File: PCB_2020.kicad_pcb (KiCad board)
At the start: 2 copper layers, 109.5 x 88 mm, 27 parts, among them IC1 LM358N, Q1 100V/17A, Q2 100V/17A, Q3 100V/17A, Q4 100V/17A, Q5 100V/17A, Q6 100V/17A, U1 AMP_DUE_SCH

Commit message: Updating PCB
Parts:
- added G***: LOGO, Image:Silk_Small_P, F.Cu at (252.7, 103.9)

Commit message: Reworked PCB
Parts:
- removed G***: LOGO, Image:Silk_Small_P
- added C1: 0.022uF, Capacitor_SMD:C_0805_2012Metric_Pad1.18x1.45mm_HandSolder, F.Cu at (169.2, 85.7)
- added C3: 0.022uF, Capacitor_SMD:C_0805_2012Metric_Pad1.18x1.45mm_HandSolder, F.Cu at (169.2, 81.5)
- added R3: 1000, Resistor_SMD:R_0612_1632Metric_Pad1.18x3.40mm_HandSolder, F.Cu at (190.1, 101.7)
- added R4: 1000, Resistor_SMD:R_0612_1632Metric_Pad1.18x3.40mm_HandSolder, F.Cu at (192.5, 133.3)
- added R6: 5400, Resistor_SMD:R_0612_1632Metric_Pad1.18x3.40mm_HandSolder, F.Cu at (201.7, 102.0)
- added R7: 5400, Resistor_SMD:R_0612_1632Metric_Pad1.18x3.40mm_HandSolder, F.Cu at (192.4, 122.4)
- added R8: 5000, Resistor_SMD:R_0612_1632Metric_Pad1.18x3.40mm_HandSolder, F.Cu at (196.9, 133.3)
- added R9: 1000, Resistor_SMD:R_0612_1632Metric_Pad1.18x3.40mm_HandSolder, F.Cu at (195.5, 101.4)
- added U2: TL084CN, Drivetrain_control:TL084CN, F.Cu at (194.3, 113.9)
- added U3: DRV8874, Drivetrain_control:DRV8874PWPR, F.Cu at (176.9, 82.9)
- C2, C5: footprint Capacitor_SMD:C_0805_2012Metric_Pad1.15x1.40mm_HandSolder -> Capacitor_SMD:C_0805_2012Metric_Pad1.18x1.45mm_HandSolder
- R1, R18, R2, R5: footprint Resistor_SMD:R_0805_2012Metric_Pad1.15x1.40mm_HandSolder -> Resistor_SMD:R_0612_1632Metric_Pad1.18x3.40mm_HandSolder
- moved CONN6 84.2 mm to (170.6, 77.4)
- moved C1 81.5 mm to (160.8, 88.3)
- moved C2 81.5 mm to (179.6, 115.1)
- moved C5 81.5 mm to (141.6, 89.1)
- moved CONN2 81.5 mm to (174.8, 110.6)
- moved CONN3 81.5 mm to (160.3, 65.1)
- moved CONN4 81.5 mm to (151.6, 60.0)
- moved CONN5 81.5 mm to (169.1, 118.6)
- moved CONN7 81.5 mm to (169.1, 65.1)
- moved H1 81.5 mm to (176.3, 135.8)
- moved H3 81.5 mm to (176.3, 58.9)
- moved IC1 81.5 mm to (145.1, 82.6)
- moved Q1 81.5 mm to (177.6, 119.3)
- moved Q2 81.5 mm to (164.1, 108.1)
- moved Q3 81.5 mm to (156.3, 108.3)
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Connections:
- U1 pad 1: (no net) -> Net-(U1-Pad1)
- U1 pad 10: (no net) -> Net-(U1-Pad10)
- U1 pad 11: (no net) -> Net-(U1-Pad11)
- U1 pad 12: (no net) -> Net-(U1-Pad12)
- U1 pad 13: (no net) -> Net-(U1-Pad13)
- U1 pad 14: (no net) -> Net-(U1-Pad14)
- U1 pad 15: (no net) -> Net-(U1-Pad15)
- U1 pad 16: (no net) -> Net-(U1-Pad16)
- U1 pad 17: (no net) -> Net-(U1-Pad17)
- U1 pad 18: (no net) -> Brake_PWM_1
- U1 pad 19: (no net) -> Brake_PWM_2
- U1 pad 2: (no net) -> Net-(U1-Pad2)
- U1 pad 20: (no net) -> STEERING
- U1 pad 21: THROTTLE -> Net-(U1-Pad21)
- U1 pad 22: (no net) -> Net-(U1-Pad22)
- U1 pad 23: (no net) -> Net-(U1-Pad23)
- U1 pad 24: (no net) -> +12V
- U1 pad 25: (no net) -> Net-(U1-Pad25)
- U1 pad 26: (no net) -> Net-(U1-Pad26)
- U1 pad 27: (no net) -> Net-(U1-Pad27)
- U1 pad 28: (no net) -> SCIB_TX
- U1 pad 29: (no net) -> Net-(U1-Pad29)
- U1 pad 3: (no net) -> Net-(U1-Pad3)
- U1 pad 30: (no net) -> Net-(U1-Pad30)
- U1 pad 31: (no net) -> Net-(U1-Pad31)
- U1 pad 32: (no net) -> Net-(U1-Pad32)
- U1 pad 33: (no net) -> Net-(U1-Pad33)
- U1 pad 34: (no net) -> THROTTLE
- U1 pad 35: (no net) -> Net-(U1-Pad35)
- U1 pad 36: (no net) -> SCIB_RX
- U1 pad 37: (no net) -> Net-(U1-Pad37)
- U1 pad 38: (no net) -> Net-(U1-Pad38)
- U1 pad 39: (no net) -> Net-(U1-Pad39)
- U1 pad 4: (no net) -> Net-(U1-Pad4)
- U1 pad 40: (no net) -> Net-(U1-Pad40)
- U1 pad 41: (no net) -> GND
- U1 pad 42: (no net) -> GND
- U1 pad 43: (no net) -> Net-(U1-Pad43)
- U1 pad 44: REV_CTL -> Net-(U1-Pad44)
- U1 pad 45: (no net) -> Net-(U1-Pad45)
- U1 pad 46: (no net) -> INPUT_A+_CTL
- U1 pad 47: EN+_CTL -> Net-(U1-Pad47)
- U1 pad 48: (no net) -> Net-(U1-Pad48)
- U1 pad 49: (no net) -> Net-(U1-Pad49)
- U1 pad 5: +5V -> Net-(U1-Pad5)
- U1 pad 50: INPUT_A+_CTL -> Net-(U1-Pad50)
- U1 pad 51: (no net) -> Net-(U1-Pad51)
- U1 pad 52: (no net) -> Net-(U1-Pad52)
- U1 pad 53: FS1_CTL -> EN+_CTL
- U1 pad 54: (no net) -> Net-(U1-Pad54)
- U1 pad 55: (no net) -> Net-(U1-Pad55)
- U1 pad 56: FWD_CTL -> Net-(U1-Pad56)
- U1 pad 57: (no net) -> Net-(U1-Pad57)
- U1 pad 58: (no net) -> Net-(U1-Pad58)
- U1 pad 59: (no net) -> REV_CTL
- U1 pad 6: GND -> Net-(U1-Pad6)
- U1 pad 60: (no net) -> Net-(U1-Pad60)
- U1 pad 61: (no net) -> Net-(U1-Pad61)
- U1 pad 62: (no net) -> Net-(U1-Pad62)
- U1 pad 63: (no net) -> Net-(U1-Pad63)
- U1 pad 64: STEERING -> Net-(U1-Pad64)
- U1 pad 65: Brake_PWM_2 -> Net-(U1-Pad65)
- U1 pad 66: Brake_PWM_1 -> +5V
- U1 pad 67: (no net) -> KS1_CTL
- U1 pad 68: (no net) -> Net-(U1-Pad68)
- U1 pad 69: (no net) -> Net-(U1-Pad69)
- U1 pad 7: GND -> Net-(U1-Pad7)
- U1 pad 70: (no net) -> Net-(U1-Pad70)
- U1 pad 71: (no net) -> Net-(U1-Pad71)
- U1 pad 72: (no net) -> Net-(U1-Pad72)
- U1 pad 73: (no net) -> Net-(U1-Pad73)
- U1 pad 74: (no net) -> FWD_CTL
- U1 pad 75: (no net) -> Net-(U1-Pad75)
- U1 pad 76: (no net) -> Net-(U1-Pad76)
- U1 pad 77: (no net) -> Net-(U1-Pad77)
- U1 pad 78: (no net) -> Net-(U1-Pad78)
- U1 pad 79: (no net) -> Net-(U1-Pad79)
- U1 pad 8: +12V -> Net-(U1-Pad8)
- U1 pad 80: (no net) -> FS1_CTL
- U1 pad 81: (no net) -> Net-(U1-Pad81)
- U1 pad 82: (no net) -> Net-(U1-Pad82)
- U1 pad 83: (no net) -> Net-(U1-Pad83)
- U1 pad 84: (no net) -> Net-(U1-Pad84)
- U1 pad 85: (no net) -> Net-(U1-Pad85)
- U1 pad 9: (no net) -> Net-(U1-Pad9)
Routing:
- net FS1_CTL: track 50.9 -> 184.6 mm
- net THROTTLE: track 36.3 -> 158.3 mm
- net +3V3: track 110.1 -> 221.5 mm
- net INPUT_A+_CTL: track 64.9 -> 135.2 mm
- net STEERING: track 119.8 -> 51.5 mm
- net FWD_CTL: track 66.9 -> 134.5 mm
- net +5V: track 18.2 -> 78.4 mm
- net Net-(R3-Pad2): track 0.00 -> 55.2 mm
- net Net-(R4-Pad1): track 0.00 -> 46.8 mm
- net REV_CTL: track 39.6 -> 78.1 mm
- net GND: track 10.9 -> 46.6 mm, vias 4 -> 10
- net EN+_CTL: track 51.4 -> 83.9 mm
- net /LAUNCHXL-F28379D Breakout/THROTTLE_MC: track 48.6 -> 80.7 mm
- net Net-(R3-Pad1): track 0.00 -> 27.6 mm
- net /LAUNCHXL-F28379D Breakout/Brake_Out_2: track 16.3 -> 28.6 mm
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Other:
- board size 109.5 x 88 mm -> 127.5 x 88 mm
- net class Power: trace_width 1.25 -> 0.35

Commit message: Updated PCB
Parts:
- removed IC1: LM358N, Package_DIP:DIP-8_W7.62mm_Socket
- moved C1 10.9 mm to (150.0, 88.8)
- moved R4 3.22 mm to (189.4, 132.3)
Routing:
- net +12V: track 5.29 -> 57.4 mm, vias 0 -> 5
- net THROTTLE: track 158.3 -> 124.1 mm
- net EN+_CTL: track 83.9 -> 117.4 mm
- net /LAUNCHXL-F28379D Breakout/THROTTLE_MC: track 80.7 -> 72.2 mm
- net Net-(IC1-Pad6): track 8.06 -> 2.45 mm
- net GND: track 46.6 -> 48.9 mm, vias 10 -> 11
- net Net-(R4-Pad1): track 46.8 -> 45.9 mm

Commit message: Working on PCB Routing for LoRa
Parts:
- removed the C1 at (169.2, 85.7)
- removed the C1 at (150.0, 88.8)
- removed the R3 at (190.1, 101.7)
- removed the R3 at (158.1, 90.6)
- removed the R4 at (189.4, 132.3)
- removed the R4 at (158.1, 86.1)
- added C1: 0.1uF, Capacitor_SMD:C_0805_2012Metric_Pad1.15x1.40mm_HandSolder, F.Cu at (130.5, 65.0)
- added C1: 0.022uF, Capacitor_SMD:C_0805_2012Metric_Pad1.18x1.45mm_HandSolder, F.Cu at (146.1, 92.8)
- added R3: 3k, Resistor_SMD:R_0805_2012Metric_Pad1.15x1.40mm_HandSolder, F.Cu at (152.2, 87.7)
- added R3: 1000, Resistor_SMD:R_0612_1632Metric_Pad1.18x3.40mm_HandSolder, F.Cu at (160.5, 64.8)
- added R4: 6.8k, Resistor_SMD:R_0805_2012Metric_Pad1.15x1.40mm_HandSolder, F.Cu at (152.2, 83.2)
- added R4: 1000, Resistor_SMD:R_0612_1632Metric_Pad1.18x3.40mm_HandSolder, F.Cu at (154.2, 92.0)
- added U4: LoRa, Drivetrain_control:LoRa, F.Cu at (235.0, 102.2)
- moved U1 83.0 mm to (196.1, 99.7)
- moved CONN7 77.4 mm to (102.0, 103.9), turned to 0 degrees
- moved CONN3 75.7 mm to (236.0, 66.8)
- moved CONN2 64.9 mm to (144.7, 53.1), turned to 270 degrees
- moved R6 58.9 mm to (155.8, 65.0)
- moved U2 53.7 mm to (157.7, 74.5)
- moved R7 53.7 mm to (155.8, 83.1)
- moved R8 53.6 mm to (161.6, 93.0)
- moved R2 52.6 mm to (150.2, 57.3), turned to 180 degrees
- moved H1 49.1 mm to (225.3, 133.6)
- moved H3 49.1 mm to (225.3, 56.6)
- moved H2 49.1 mm to (131.3, 133.6)
- moved H4 49.1 mm to (131.3, 56.6)
- moved R9 48.0 mm to (164.4, 64.8)
- moved R18 44.8 mm to (150.2, 61.6), turned to 180 degrees
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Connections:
- U1 pad 83: Net-(U1-Pad83) -> +3V3
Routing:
- net +3V3: track 221.5 -> 12.4 mm, vias 1 -> 0
- net THROTTLE: track 124.1 -> 0.00 mm
- net FWD_CTL: track 134.5 -> 44.3 mm
- net EN+_CTL: track 117.4 -> 29.6 mm
- net Brake_PWM_1: track 93.8 -> 14.6 mm
- net +5V: track 78.4 -> 0.00 mm
- net Brake_PWM_2: track 90.9 -> 16.5 mm
- net INPUT_A+_CTL: track 135.2 -> 66.7 mm
- net /LAUNCHXL-F28379D Breakout/INPUT_A+: track 16.7 -> 82.6 mm
- net FS1_CTL: track 184.6 -> 119.4 mm
- net /LAUNCHXL-F28379D Breakout/INPUT_B+: track 22.8 -> 84.1 mm
- net +12V: track 57.4 -> 5.29 mm, vias 5 -> 0
- net /LAUNCHXL-F28379D Breakout/EN+: track 26.3 -> 75.0 mm
- net REV_CTL: track 78.1 -> 31.0 mm
- net STEERING: track 51.5 -> 93.2 mm, vias 0 -> 1
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- removed copper zone on F.Cu, net +12V
- removed copper zone on B.Cu, net GND
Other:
- board size 127.5 x 88 mm -> 125.4 x 87.9 mm

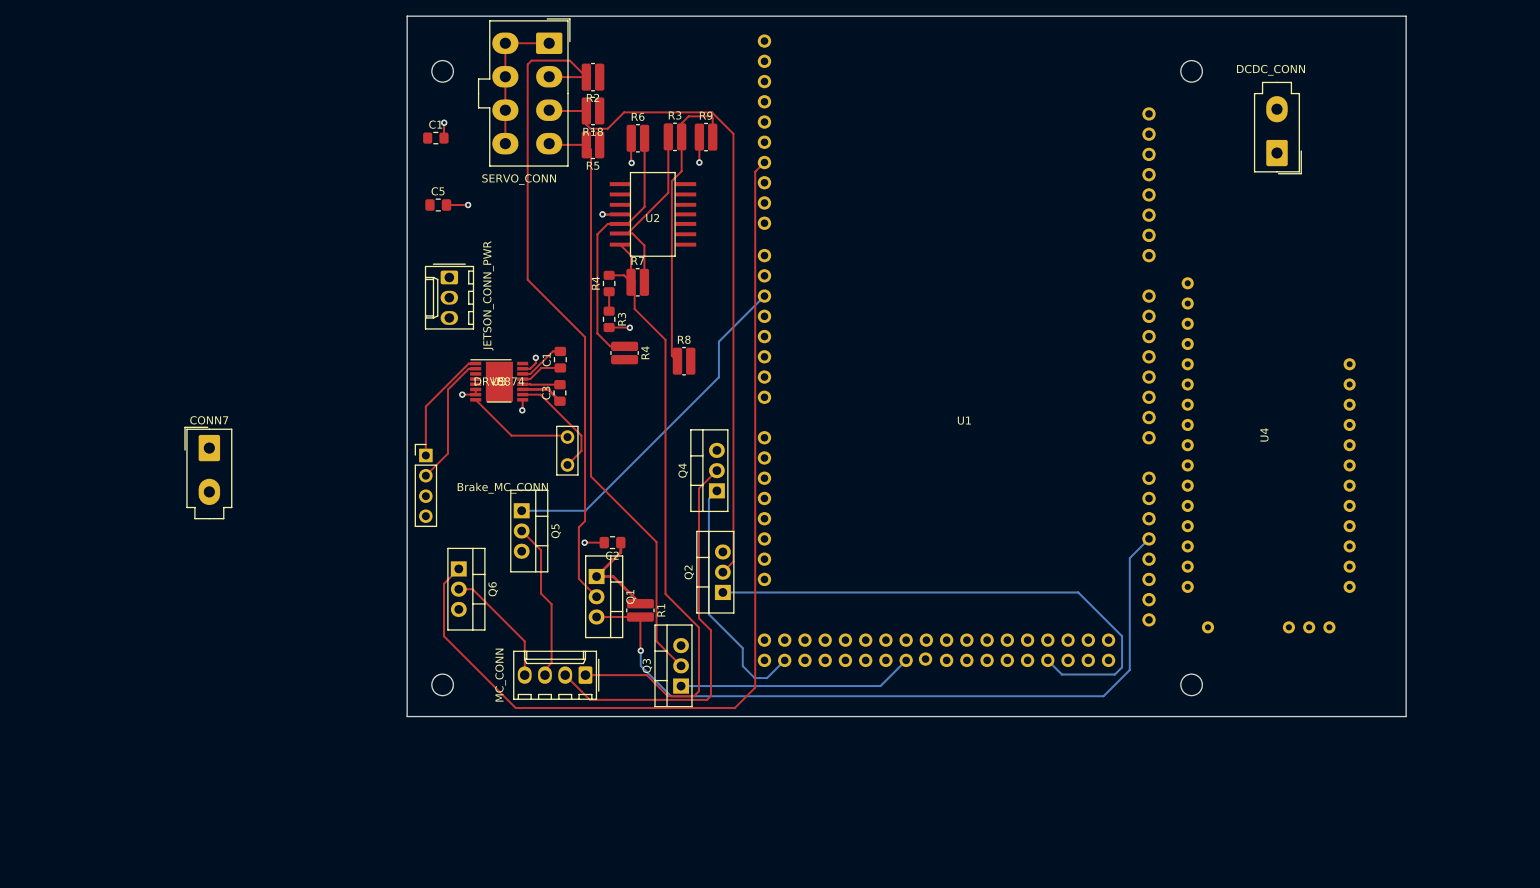
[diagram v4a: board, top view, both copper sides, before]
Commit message: Updating PCB with LoRa
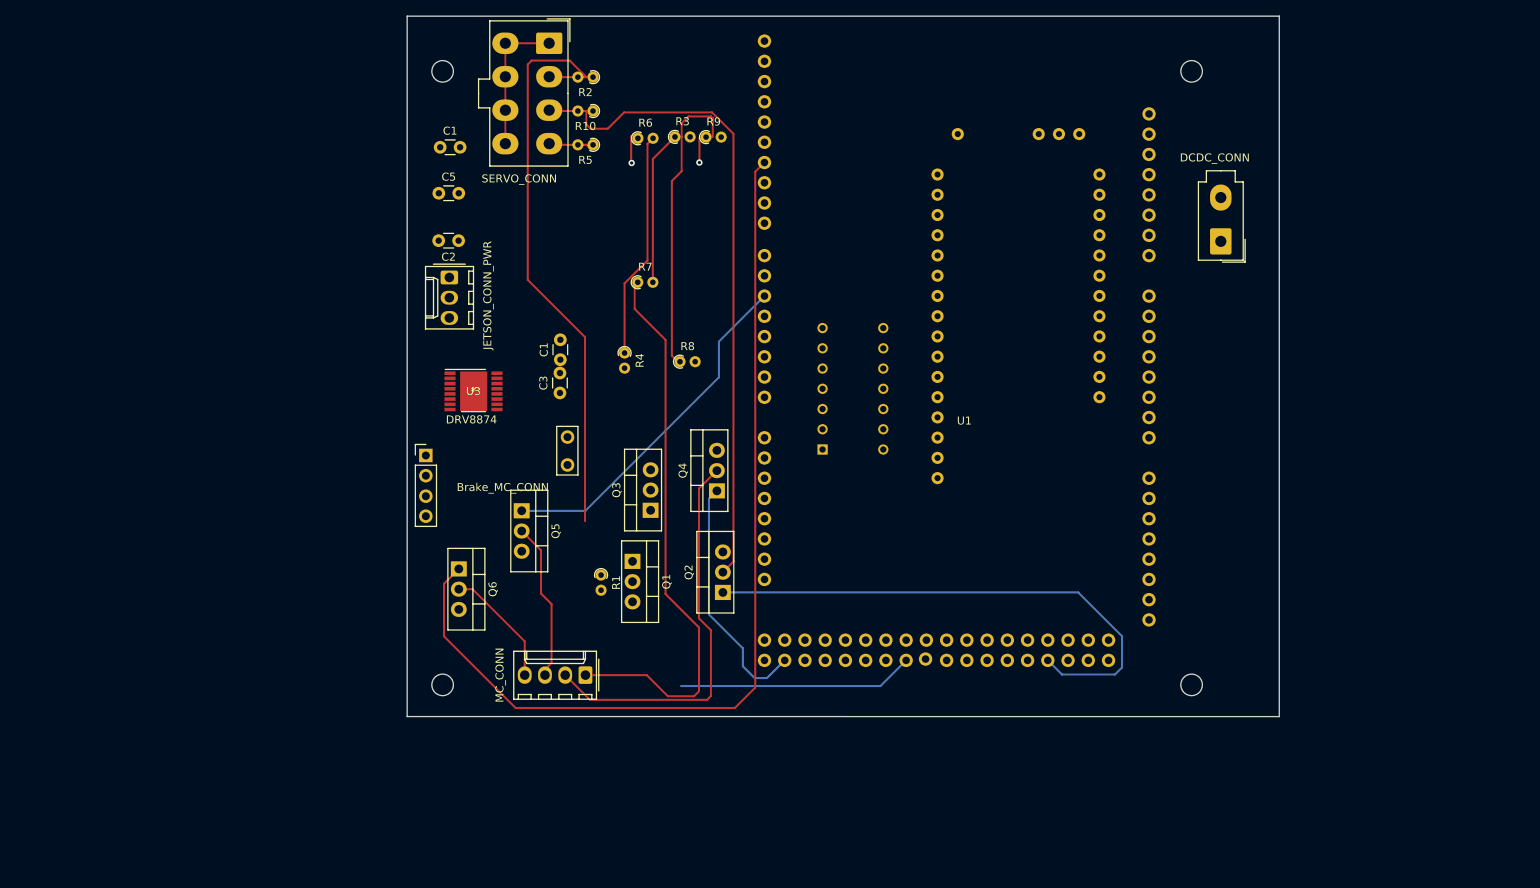
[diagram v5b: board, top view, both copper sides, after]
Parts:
- removed CONN7: Brake_CONN, Connector_Molex:Molex_Mini-Fit_Jr_5566-02A_2x01_P4.20mm_Vertical
- removed the R3 at (152.2, 87.7)
- removed the R4 at (152.2, 83.2)
- C1: value 0.1uF -> 0.022 uF; footprint Capacitor_SMD:C_0805_2012Metric_Pad1.15x1.40mm_HandSolder -> Capacitor_THT:C_Disc_D3.0mm_W1.6mm_P2.50mm
- C1, C2, C3, C5: footprint Capacitor_SMD:C_0805_2012Metric_Pad1.18x1.45mm_HandSolder -> Capacitor_THT:C_Disc_D3.0mm_W1.6mm_P2.50mm
- R1, R2, R3, R4, R5, R6, R7, R8, R9: footprint Resistor_SMD:R_0612_1632Metric_Pad1.18x3.40mm_HandSolder -> Resistor_THT:R_Axial_DIN0204_L3.6mm_D1.6mm_P1.90mm_Vertical
- R10: renamed from R18; footprint Resistor_SMD:R_0612_1632Metric_Pad1.18x3.40mm_HandSolder -> Resistor_THT:R_Axial_DIN0204_L3.6mm_D1.6mm_P1.90mm_Vertical
- U2, U4: moved to B.Cu
- moved C2 42.5 mm to (133.3, 77.8)
- moved U4 34.2 mm to (203.6, 88.6), turned to 90 degrees
- moved U2 32.3 mm to (186.6, 88.8)
- moved Q3 22.4 mm to (157.4, 111.7)
- moved CONN3 13.1 mm to (229.0, 77.9)
- moved R1 6.64 mm to (151.2, 119.8)
- moved Q1 4.89 mm to (155.2, 118.1)
- moved U3 3.44 mm to (135.2, 96.8)
- moved C5 1.48 mm to (130.8, 71.9)
- moved C1 1.28 mm to (131.0, 66.1)
- moved R8 0.51 mm to (161.1, 93.0)
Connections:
- C1 pad 1: (no net) -> Net-(C1-Pad1)
- C1 pad 2: (no net) -> Net-(C1-Pad2)
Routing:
- net STEERING: track 93.2 -> 0.00 mm, vias 1 -> 0
- net /LAUNCHXL-F28379D Breakout/EN+: track 75.0 -> 5.56 mm
- net Brake_PWM_2: track 16.5 -> 0.00 mm
- net Brake_PWM_1: track 14.6 -> 0.00 mm
- net GND: track 39.3 -> 24.7 mm, vias 8 -> 2
- net /LAUNCHXL-F28379D Breakout/Brake_Out_2: track 13.9 -> 0.00 mm
- net /LAUNCHXL-F28379D Breakout/Brake_Out_1: track 13.5 -> 0.00 mm
- net +3V3: track 12.4 -> 0.00 mm
- net /LAUNCHXL-F28379D Breakout/INPUT_B+: track 84.1 -> 73.4 mm
- net (no net): track 10.1 -> 0.00 mm, vias 2 -> 0
- net Net-(C1-Pad2): track 5.90 -> 0.00 mm
- net /LAUNCHXL-F28379D Breakout/THROTTLE_MC: track 75.8 -> 70.5 mm
- net Net-(C1-Pad1): track 5.31 -> 0.00 mm
- net +12V: track 5.29 -> 0.00 mm
- net Net-(C3-Pad2): track 4.70 -> 0.00 mm
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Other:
- board size 125.4 x 87.9 mm -> 109.5 x 87.9 mm
